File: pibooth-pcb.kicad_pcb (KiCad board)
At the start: 2 copper layers, 54 x 35 mm, 22 parts, among them J1 Rasbpberry, J2 UART, J3 LED1, J4 LED3, J5 SW1, J6 SW2, J7 LED2, J8 LED4, SW1 SW_Push, SW2 SW_Push

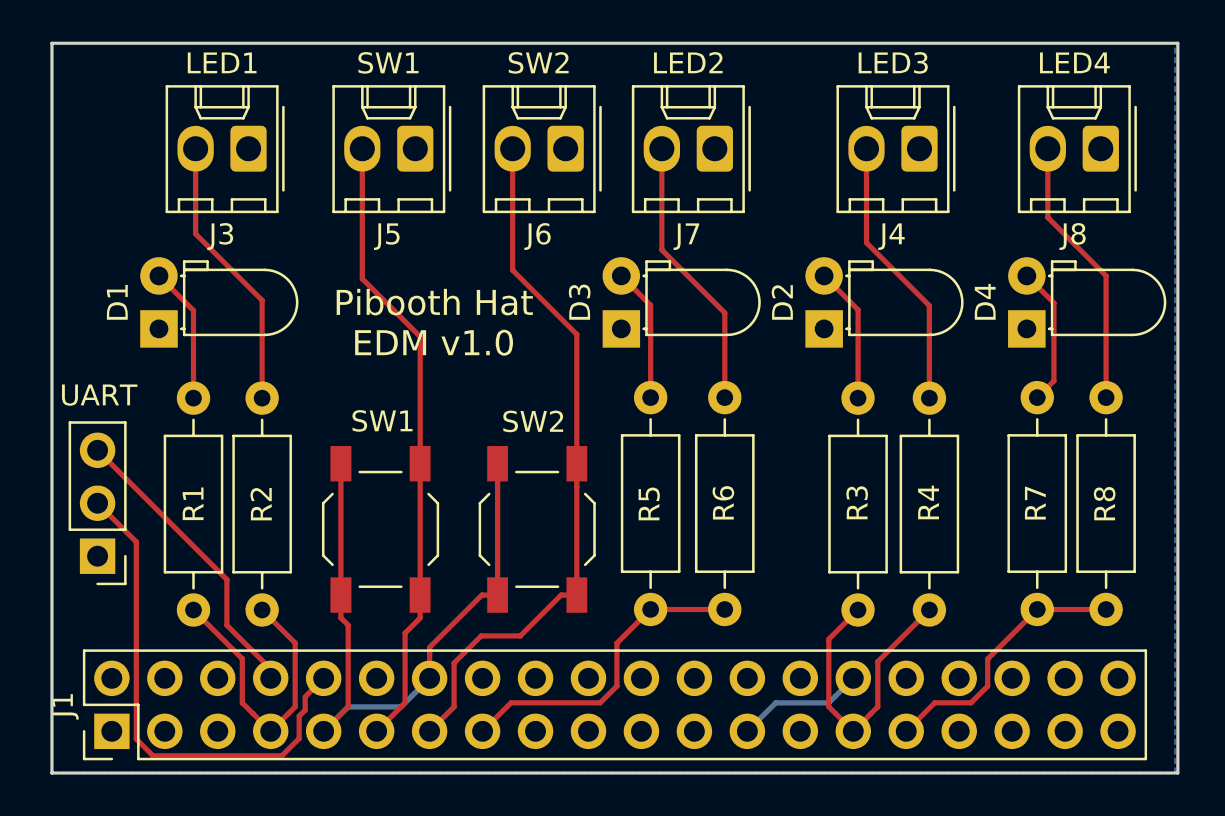
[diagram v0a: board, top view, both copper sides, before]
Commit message: Fix wrong pi header orientation
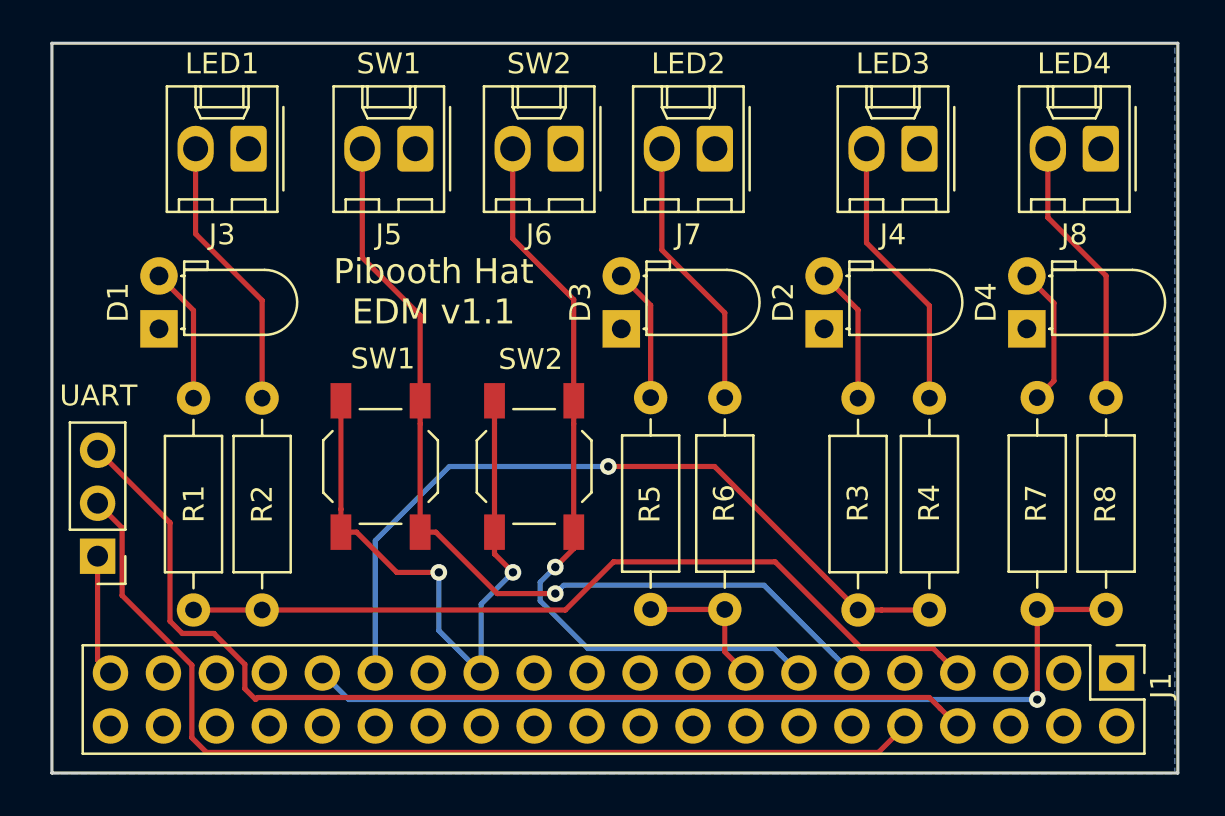
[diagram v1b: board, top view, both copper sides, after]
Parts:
- moved J1 48.3 mm to (163.1, 108.2), turned to 270 degrees
- moved SW2 3.02 mm to (135.1, 98.3)
- moved SW1 3.02 mm to (127.8, 98.3)
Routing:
- net /UART_TX: track 14.4 -> 50.3 mm
- net /LED4: track 12.8 -> 42.4 mm, vias 0 -> 1
- net /LED1: track 14.3 -> 39.8 mm
- net /UART_RX: track 23.9 -> 48.1 mm
- net /LED3: track 14.2 -> 37.3 mm, vias 0 -> 1
- net /BUTTON1: track 30.0 -> 43.4 mm, vias 0 -> 1
- net /LED2: track 15.2 -> 7.02 mm
- net /BUTTON2: track 33.7 -> 37.4 mm, vias 0 -> 1
- net GND: track 37.9 -> 37.5 mm, vias 0 -> 2
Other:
- board text added: "Pibooth Hat EDM v1.1"
- board text removed: "Pibooth Hat EDM v1.0"
